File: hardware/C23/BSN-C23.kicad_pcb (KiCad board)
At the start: 4 copper layers, 34 x 34 mm, 44 parts, among them J1 Conn_Coaxial_Small, U1 nRF54L05-QFXX, U2 SHTC3, U3 HDC2010, X1 32MHz, X2 32.768kHz

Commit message: Cleaned up libraries for both variants
Renamed the project libraries to BSN-N54 / BSN-C23 and updated lib tables and all references, removed Nordic parts and the unused 40-pin CC2340 package from the C23 library, synced Antenna symbol fields to N54, updated READMEs.
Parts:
- AE1: footprint BLE_Sensor_Node:AANI-CH-0138-Q-T -> BSN-C23:AANI-CH-0138-Q-T
- U1: footprint BLE_Sensor_Node:VQFN-48-1EP_6x6mm_P0.4mm_EP4.1x4.1mm_ThermalVias -> BSN-C23:VQFN-48-1EP_6x6mm_P0.4mm_EP4.1x4.1mm_ThermalVias
- U3: footprint BLE_Sensor_Node:HDC2010 -> BSN-C23:HDC2010
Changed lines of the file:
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@@
 		)
 	)
-	(footprint "BLE_Sensor_Node:HDC2010"
+	(footprint "BSN-C23:HDC2010"
 		(layer "F.Cu")
 		(at 159.2 106 90)
@@
 		)
 	)
-	(footprint "BLE_Sensor_Node:VQFN-48-1EP_6x6mm_P0.4mm_EP4.1x4.1mm_ThermalVias"
+	(footprint "BSN-C23:VQFN-48-1EP_6x6mm_P0.4mm_EP4.1x4.1mm_ThermalVias"
 		(locked yes)
 		(layer "F.Cu")
@@
 		)
 		(embedded_fonts no)
-		(model "${KIPRJMOD}/library/3d_models/QFN-48-1EP_6x6_P04mm.STEP"
+		(model "${KIPRJMOD}/library/3d_models/VQFN-48-1EP_6x6mm_P0.4mm_EP4.1x4.1mm.step"
 			(offset
 				(xyz 0 0 0)
@@
 		)
 	)
-	(footprint "BLE_Sensor_Node:AANI-CH-0138-Q-T"
+	(footprint "BSN-C23:AANI-CH-0138-Q-T"
 		(layer "F.Cu")
 		(at 150 84.75)

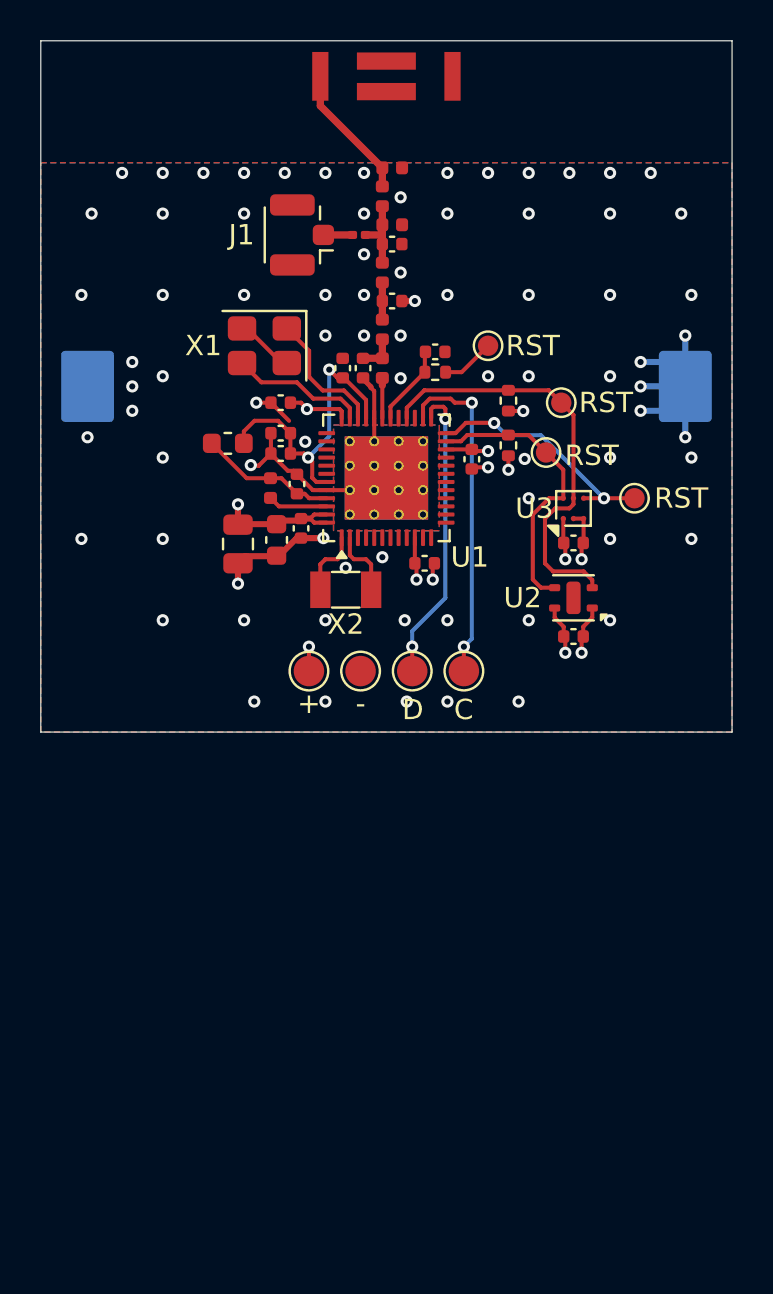
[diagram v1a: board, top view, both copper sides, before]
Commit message: Started C23 varant layout
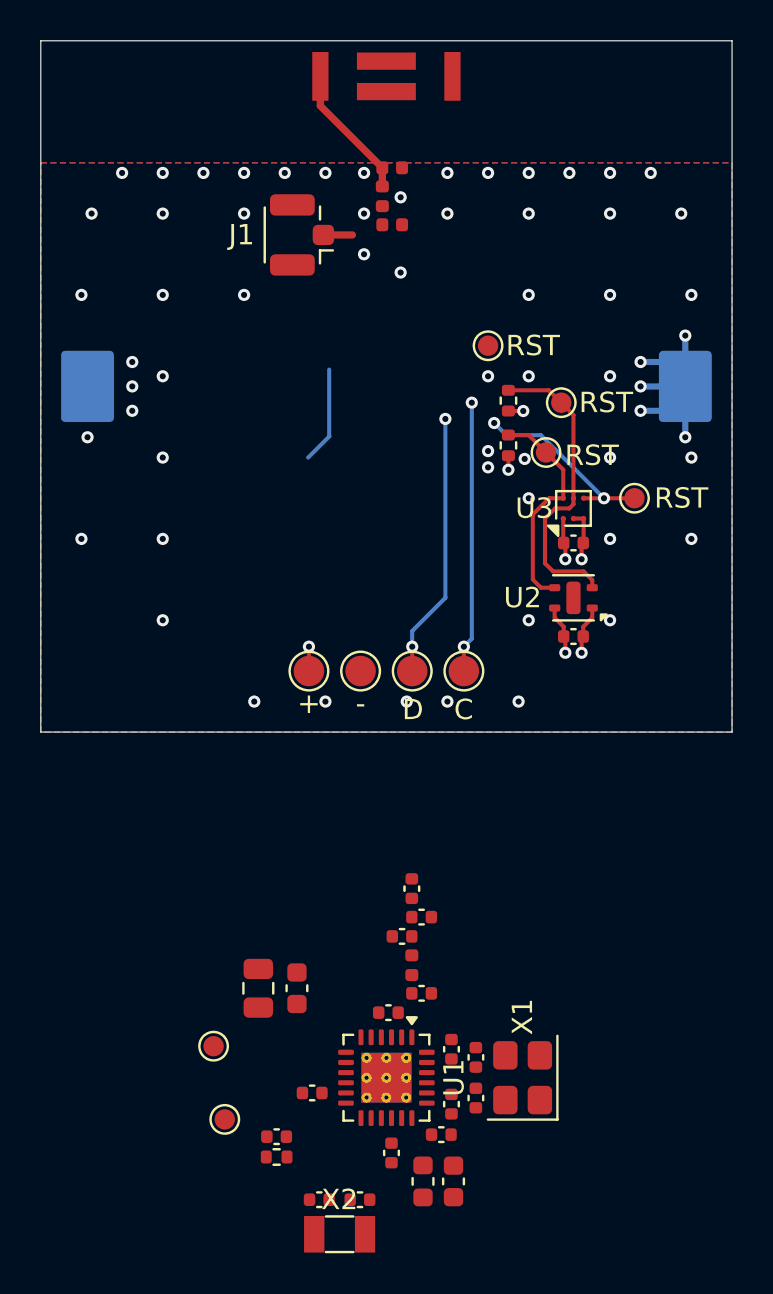
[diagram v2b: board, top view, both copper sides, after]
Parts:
- removed the C16 at (150.3, 93.0)
- removed the C5 at (144.8, 100.8)
- removed the C7 at (144.8, 103.3)
- removed FB1: 100R@100MHz, Inductor_SMD:L_0603_1608Metric
- removed the L3 at (149.8, 97.2)
- removed the L4 at (149.8, 94.4)
- removed R4: R, Resistor_SMD:R_0201_0603Metric
- added C10: 10u, Capacitor_SMD:C_0603_1608Metric, F.Cu at (153.3, 139.1)
- added C11: 100n, Capacitor_SMD:C_0402_1005Metric, F.Cu at (150.1, 130.8)
- added C12: 100n, Capacitor_SMD:C_0402_1005Metric, F.Cu at (153.2, 135.3)
- added C13: 1u, Capacitor_SMD:C_0402_1005Metric, F.Cu at (150.2, 137.7)
- added C14: C, Capacitor_SMD:C_0402_1005Metric, F.Cu at (154.4, 133.0)
- added C19: C, Capacitor_SMD:C_0402_1005Metric, F.Cu at (148.7, 140.0)
- added C20: C, Capacitor_SMD:C_0402_1005Metric, F.Cu at (146.7, 140.0)
- added TP2: TestPoint, TestPoint:TestPoint_Pad_D1.0mm, F.Cu at (141.5, 132.4)
- added TP6: TestPoint, TestPoint:TestPoint_Pad_D1.0mm, F.Cu at (142.1, 136.1)
- C15: value 2.0p -> C
- C6: value 2.2u -> 15p
- C8: value 10n -> 1.5p
- C9: value 10n -> 15p
- L1: renamed from L2; value 2.7n -> 2.8n
- L5: renamed from L1; value 4.7u -> 10u; footprint Inductor_SMD:L_0402_1005Metric -> Inductor_SMD:L_0603_1608Metric
- R3: renamed from R1; value 1k -> 100k
- U1: value nRF54L05-QFXX -> CC2340R52E0RGER; footprint BSN-C23:VQFN-48-1EP_6x6mm_P0.4mm_EP4.1x4.1mm_ThermalVias -> BSN-C23:Texas_RGE0024B_VQFN-24-1EP_4x4mm_P0.5mm_EP2.45x2.45mm_ThermalVias
- X1: value 32MHz -> 48MHz
- moved C15 39.4 mm to (154.4, 135.0), turned to -90 degrees
- moved C18 39.4 mm to (144.6, 136.9), turned to 180 degrees
- moved R3 39.4 mm to (144.6, 137.9), turned to 180 degrees
- moved X1 38.2 mm to (156.7, 134.0), turned to 90 degrees
- moved L5 34.9 mm to (151.8, 139.1), turned to 90 degrees
- moved C2 32.1 mm to (146.3, 134.8), turned to 180 degrees
- moved X2 31.7 mm to (147.7, 141.7), turned to 180 degrees
- moved C7 30.9 mm to (151.7, 129.8), turned to 0 degrees
- moved U1 29.5 mm to (150.0, 134.0), turned to -90 degrees
- moved L1 29.4 mm to (151.2, 128.5)
- moved C3 28.1 mm to (152.7, 136.8)
- moved C9 27.3 mm to (151.7, 126.1), turned to 0 degrees
- moved C4 26.7 mm to (153.2, 132.6)
- moved C8 25.5 mm to (150.8, 127.0)
- moved C1 22.1 mm to (145.6, 129.6)
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- renumbered C11 to C16, C12 to C17, C13 to C18, C4 to C2, C2 to C4, C10 to C5, C14 to C7, L6 to L2, L5 to L3, L7 to L4, R2 to R1, R3 to R2, TP6 to TP1, TP4 to TP10, TP2 to TP3, TP5 to TP4, TP3 to TP5, TP8 to TP7, TP7 to TP8, TP1 to TP9
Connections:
- C15 pad 1: Net-(C15-Pad1) -> /X48P
- C18 pad 1: Net-(U1-~{RESET}) -> /~{RESET}
- C6 pad 1: Net-(U1-DECD) -> Net-(C6-Pad1)
- C6 pad 2: GND -> Net-(C6-Pad2)
- C7 pad 1: Net-(C14-Pad1) -> Net-(U1-ANT)
- C8 pad 1: Net-(U1-DECA) -> Net-(C6-Pad2)
- C9 pad 1: Net-(U1-DECA) -> Net-(C6-Pad2)
- C9 pad 2: GND -> Net-(J1-In)
- L1 pad 2: Net-(C14-Pad1) -> Net-(C6-Pad2)
- L2 pad 1: Net-(C16-Pad1) -> Net-(C6-Pad1)
- L3 pad 2: Net-(C16-Pad1) -> Net-(C6-Pad1)
- L5 pad 1: Net-(U1-DECD) -> Net-(C10-Pad1)
- L5 pad 2: Net-(U1-DCC) -> Net-(U1-DCDC)
- R3 pad 1: Net-(U1-~{RESET}) -> /~{RESET}
- R3 pad 2: /~{RESET} -> VDD
- TP3 pad 1: Net-(U1-SWDCLK) -> Net-(U1-DIO16_SWDIO)
- TP5 pad 1: Net-(U1-SWDIO) -> Net-(U1-DIO17_SWDCK)
- U1 pad 1: /XL1 -> Net-(U1-ANT)
- U1 pad 10: VDD -> /INT
- U1 pad 11: unconnected-(U1-P2.00-Pad11) -> VDD
- U1 pad 12: unconnected-(U1-P2.01-Pad12) -> /SCL
- U1 pad 13: unconnected-(U1-P2.02-Pad13) -> /~{RESET}
- U1 pad 14: unconnected-(U1-P2.03-Pad14) -> /X32P
- U1 pad 15: unconnected-(U1-P2.04-Pad15) -> /X32N
- U1 pad 16: unconnected-(U1-P2.05-Pad16) -> Net-(U1-VDDD)
- U1 pad 17: unconnected-(U1-P2.06-Pad17) -> Net-(U1-DCDC)
- U1 pad 18: unconnected-(U1-P2.07-Pad18) -> VDD
- U1 pad 2: /XL2 -> Net-(C10-Pad1)
- U1 pad 20: unconnected-(U1-P2.09-Pad20) -> Net-(C10-Pad1)
- U1 pad 21: unconnected-(U1-P2.10-Pad21) -> /X48P
- U1 pad 22: VDD -> /X48N
- U1 pad 23: /SDA -> GND
- U1 pad 24: /INT -> VDD
- U1 pad 25: Net-(U1-SWDIO) -> GND
- U1 pad 5: unconnected-(U1-P1.04-Pad5) -> /SDA
- U1 pad 6: unconnected-(U1-P1.05-Pad6) -> /TXD
- U1 pad 7: unconnected-(U1-P1.06-Pad7) -> Net-(U1-DIO16_SWDIO)
- U1 pad 8: unconnected-(U1-P1.07-Pad8) -> Net-(U1-DIO17_SWDCK)
- U1 pad 9: unconnected-(U1-P1.08-Pad9) -> /RXD
- X1 pad 1: /XC1 -> /X48P
- X1 pad 3: /XC2 -> /X48N
- X2 pad 1: /XL2 -> /X32P
- X2 pad 2: /XL1 -> /X32N
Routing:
- net GND: track 28.1 -> 4.96 mm, vias 78 -> 58
- net Net-(U1-SWDCLK): track 16.6 -> 0.00 mm, vias 2 -> 0
- net Net-(U1-DECA): track 15.3 -> 0.00 mm, vias 2 -> 0
- net Net-(U1-SWDIO): track 14.8 -> 0.00 mm, vias 2 -> 0
- net VDD: track 32.4 -> 18.7 mm, vias 14 -> 11
- net Net-(U1-DIO16_SWDIO): track 0.00 -> 13.4 mm, vias 0 -> 2
- net Net-(U1-DIO17_SWDCK): track 0.00 -> 13.1 mm, vias 0 -> 2
- net Net-(U1-DECD): track 6.77 -> 0.00 mm
- net /XC2: track 6.72 -> 0.00 mm
- net /XC1: track 6.48 -> 0.00 mm
- net /SCL: track 20.9 -> 15.0 mm
- net (no net): track 0.00 -> 4.76 mm
- net Net-(U1-~{RESET}): track 3.97 -> 0.00 mm
- net Net-(C16-Pad1): track 3.61 -> 0.00 mm
- net /XL2: track 3.35 -> 0.00 mm
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
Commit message: Progress on C23 layout & Routing
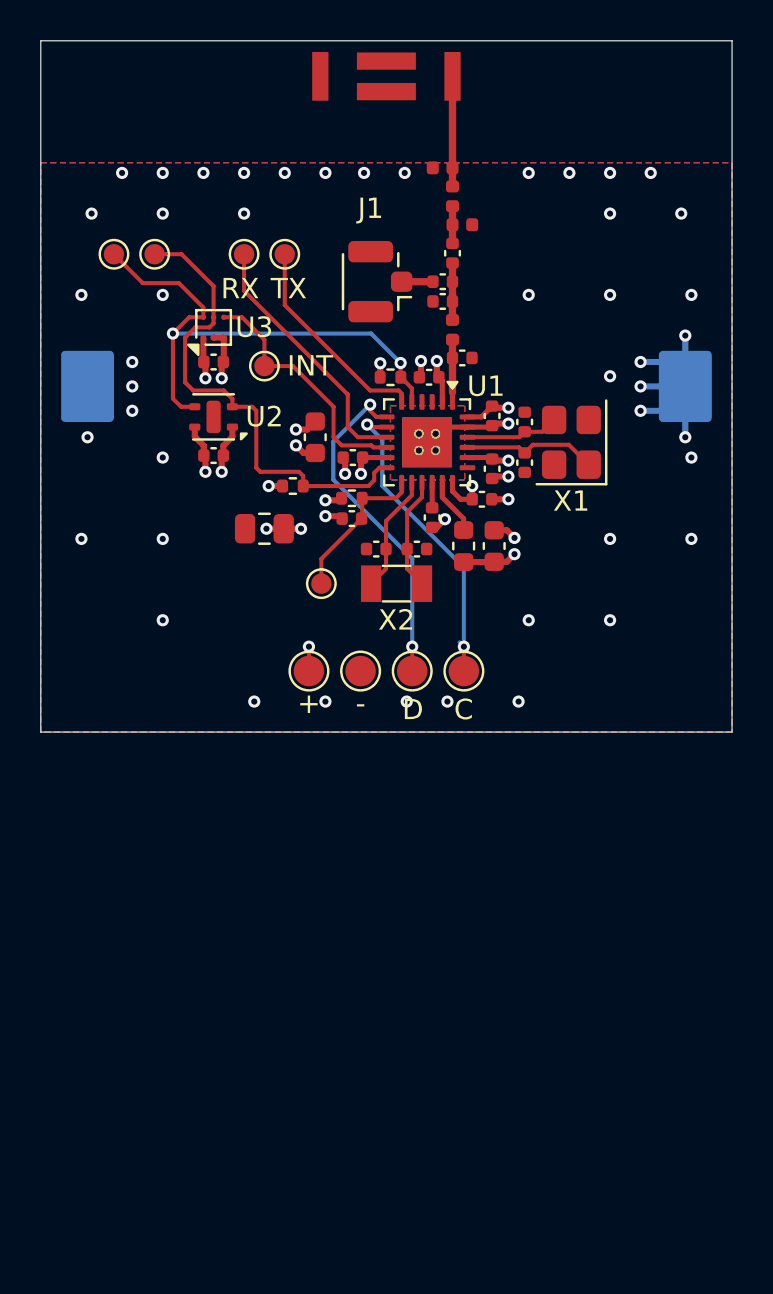
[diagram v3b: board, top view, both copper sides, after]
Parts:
- moved TP6 42.6 mm to (143.0, 93.5), turned to 180 degrees
- moved TP2 39.1 mm to (145.0, 93.5), turned to 180 degrees
- moved R3 32.6 mm to (148.3, 105.5)
- moved C19 32.1 mm to (151.5, 108.0)
- moved C20 32.1 mm to (149.5, 108.0)
- moved X2 32.1 mm to (150.5, 109.7)
- moved C14 31.3 mm to (156.8, 101.8)
- moved C15 31.3 mm to (156.8, 103.8)
- moved X1 31.3 mm to (159.1, 102.8)
- moved C11 31.3 mm to (152.1, 99.5)
- moved C12 31.3 mm to (155.2, 104.0)
- moved C3 31.3 mm to (154.7, 105.5)
- moved C10 31.3 mm to (155.3, 107.8)
- moved C2 31.3 mm to (148.3, 103.5)
- moved C6 31.3 mm to (153.2, 93.5)
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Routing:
- net /SDA: track 11.1 -> 26.2 mm, vias 0 -> 2
- net /RXD: track 0.00 -> 12.7 mm
- net GND: track 4.96 -> 16.6 mm, vias 58 -> 52
- net /TXD: track 0.00 -> 10.5 mm
- net VDD: track 18.7 -> 28.8 mm, vias 11 -> 17
- net /SCL: track 15.0 -> 24.0 mm
- net /~{RESET}: track 0.00 -> 7.57 mm
- net Net-(C10-Pad1): track 0.00 -> 6.86 mm, vias 0 -> 3
- net /X48P: track 0.00 -> 6.65 mm
- net /X32P: track 0.00 -> 5.79 mm
- net /X32N: track 0.00 -> 5.57 mm
- net (no net): track 4.76 -> 0.00 mm
- net /X48N: track 0.00 -> 4.61 mm
- net Net-(U1-DIO16_SWDIO): track 13.4 -> 16.7 mm
- net Net-(U1-ANT): track 0.00 -> 3.06 mm
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- added copper zone on In2.Cu, net Net-(C10-Pad1)
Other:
- board text added: "INT"
- board text added: "RX"
- board text added: "TX"
- board text removed: "RST"

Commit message: More vias & SDA lables on silkscreen
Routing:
- net GND: track 16.6 -> 18.1 mm, vias 52 -> 85
- net Net-(U1-DIO16_SWDIO): track 16.7 -> 17.2 mm
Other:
- board text added: "SCL"
- board text added: "SDA"

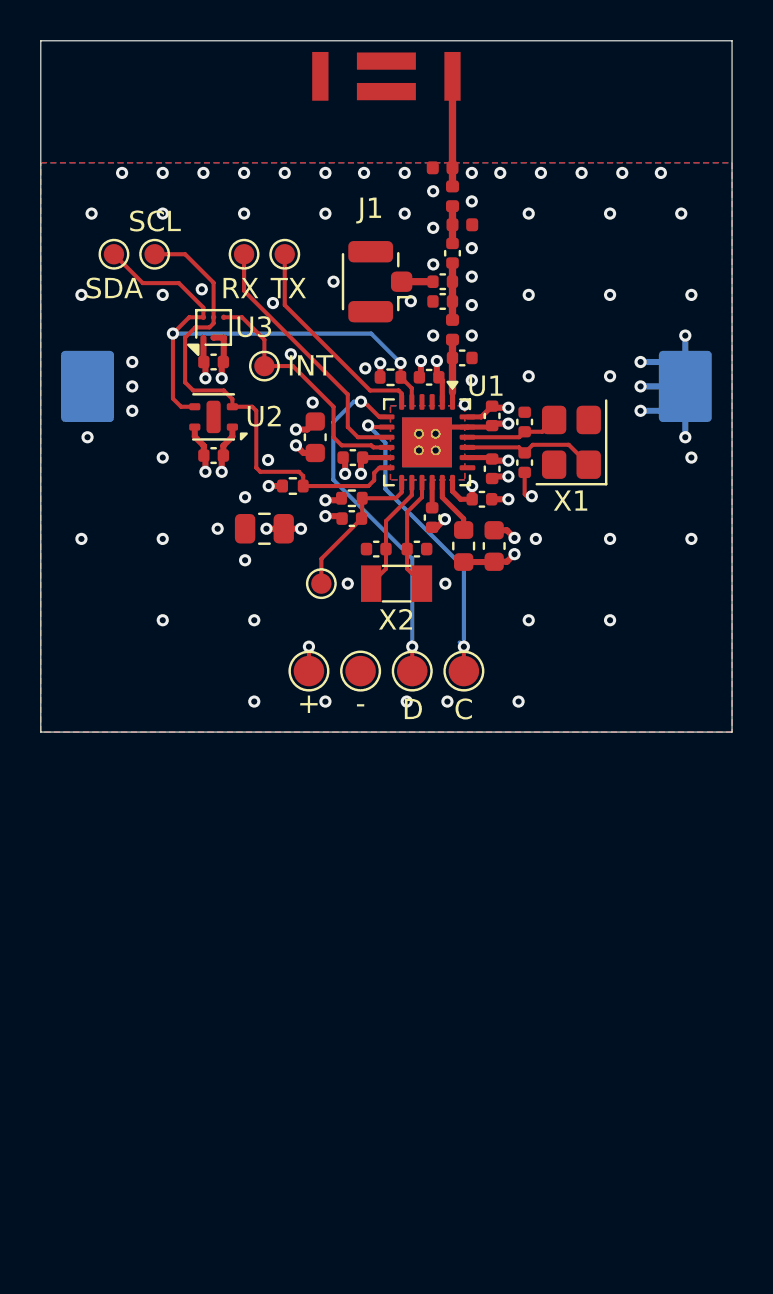
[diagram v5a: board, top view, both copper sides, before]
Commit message: Rounded tracks
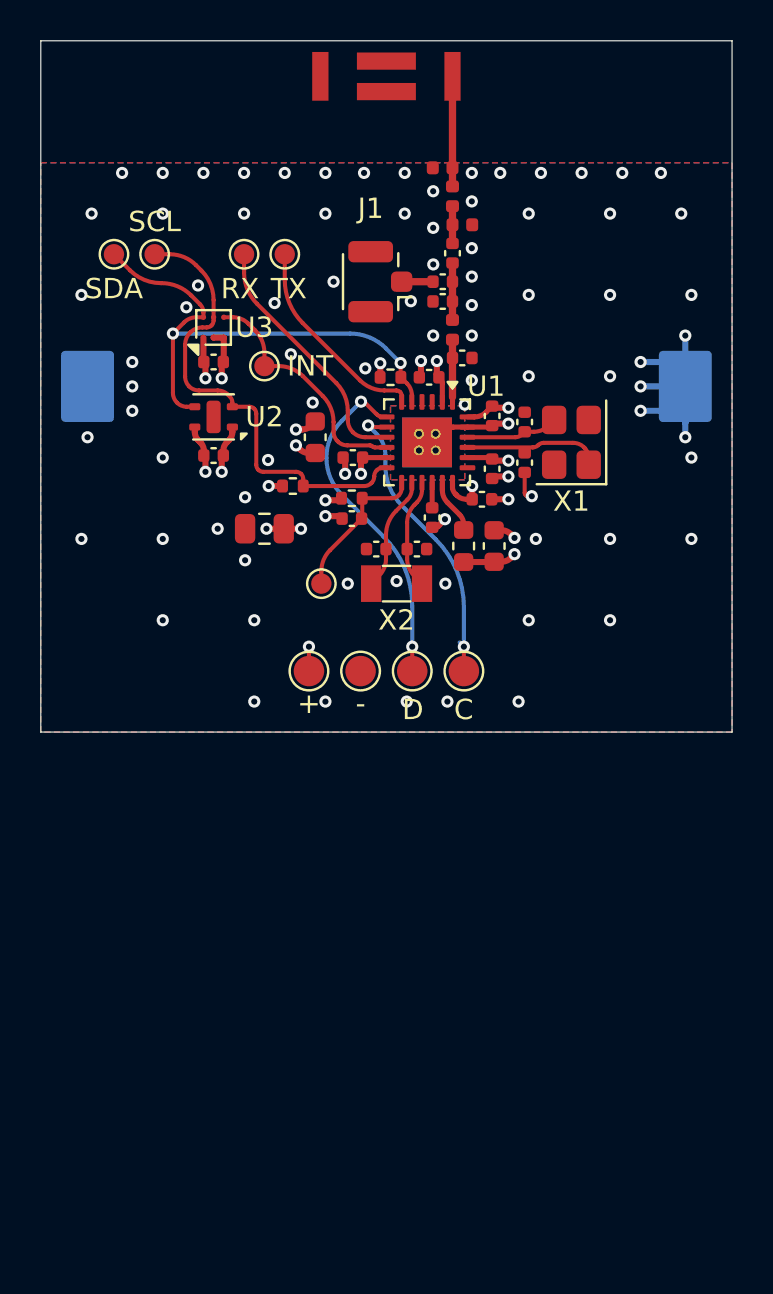
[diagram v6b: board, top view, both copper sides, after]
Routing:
- net VDD: track 28.8 -> 31.0 mm
- net /SCL: track 24.1 -> 23.5 mm
- net GND: track 18.1 -> 17.8 mm, vias 85 -> 86

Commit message: Small routing / copper pours fixes
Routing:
- net GND: track 17.8 -> 27.3 mm, vias 86 -> 87
- net VDD: track 31.0 -> 28.4 mm
